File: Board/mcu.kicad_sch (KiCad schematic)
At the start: 20 parts, among them J2 Conn_01x03_Pin, Q1 BSS138, U2 RP2040

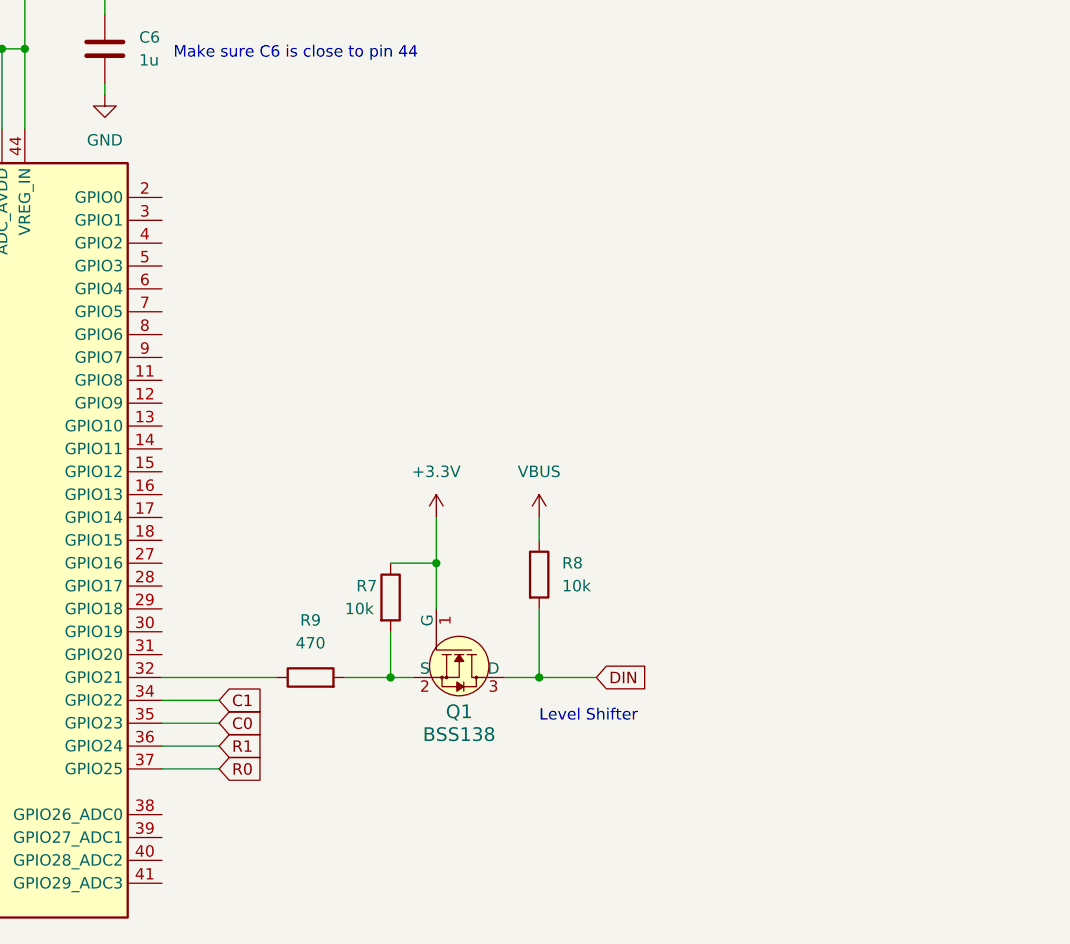
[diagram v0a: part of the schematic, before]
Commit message: Change led decoupler type
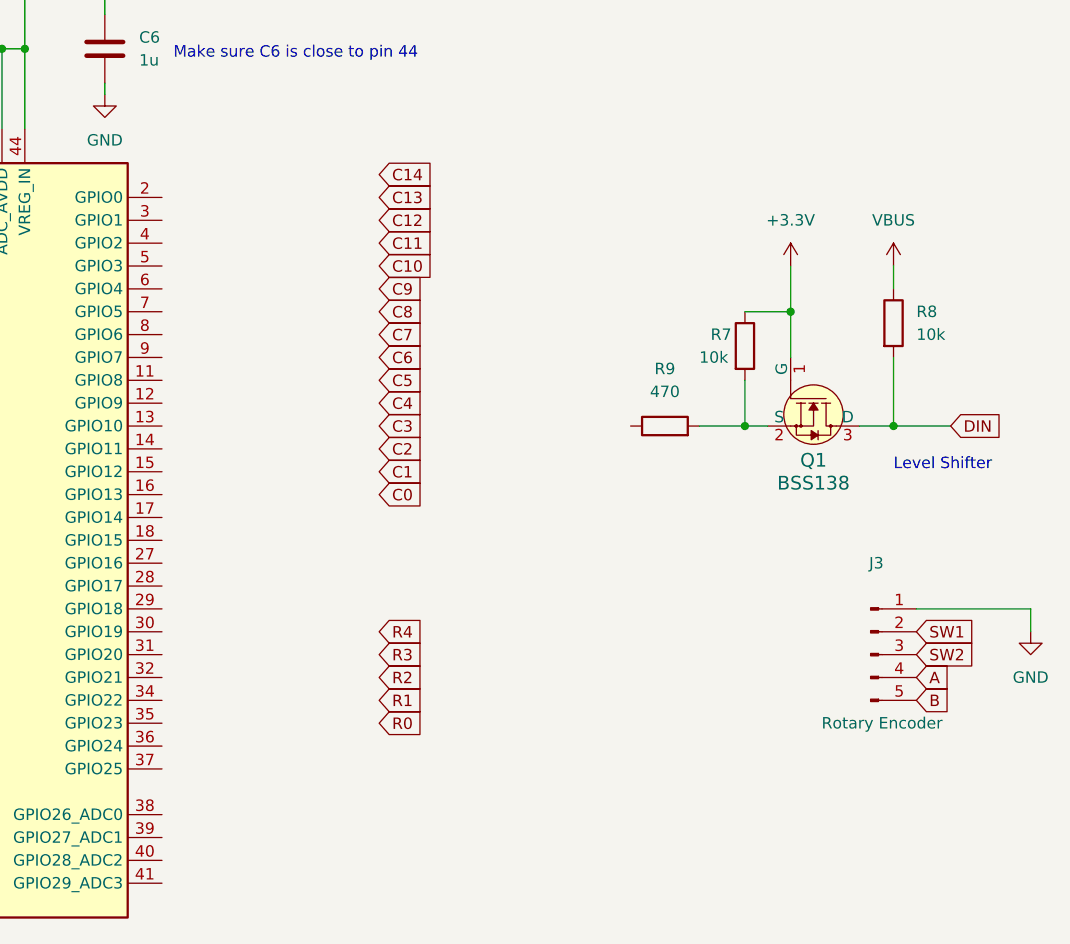
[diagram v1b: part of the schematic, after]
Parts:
- added J3: Conn_01x05_Pin, Connector_PinHeader_2.54mm:PinHeader_1x05_P2.54mm_Vertical, symbol Connector:Conn_01x05_Pin
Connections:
- net C0: no longer U2.35 (GPIO23)
- net C1: no longer U2.34 (GPIO22)
- net GND: now also J3.1 (Pin_1)
- net R0: no longer U2.37 (GPIO25)
- net R1: no longer U2.36 (GPIO24)
- net at R9.1: no longer U2.32 (GPIO21)
- new net A: J3.4 (Pin_4)
- new net B: J3.5 (Pin_5)
- new net SW1: J3.2 (Pin_2)
- new net SW2: J3.3 (Pin_3)
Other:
- moved on the sheet: Q1, R7, R8, R9

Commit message: Backing up"
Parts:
- Q1: footprint digikey-footprints:SOT-23-3 -> Package_TO_SOT_SMD:SOT-23-3
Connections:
- net A: now also U2.35 (GPIO23)
- net B: now also U2.34 (GPIO22)
- net SW1: now also U2.37 (GPIO25)
- net SW2: now also U2.36 (GPIO24)
- net LED: now reaches R9.1
- net LED: now also U2.32 (GPIO21)
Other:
- moved on the sheet: J3
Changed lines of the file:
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@@
     (stroke (width 0) (type default))
   )
-  (wire (pts (xy 232.41 125.73) (xy 232.41 128.27))
+  (wire (pts (xy 172.72 148.59) (xy 172.72 151.13))
     (stroke (width 0) (type default))
   )
@@
     (stroke (width 0) (type default))
   )
+  (wire (pts (xy 135.89 138.43) (xy 139.7 138.43))
+    (stroke (width 0) (type default))
+  )
   (wire (pts (xy 189.23 41.91) (xy 201.93 41.91))
     (stroke (width 0) (type default))
@@
     (stroke (width 0) (type default))
   )
+  (wire (pts (xy 135.89 140.97) (xy 139.7 140.97))
+    (stroke (width 0) (type default))
+  )
   (wire (pts (xy 118.11 63.5) (xy 118.11 72.39))
     (stroke (width 0) (type default))
@@
     (stroke (width 0) (type default))
   )
+  (wire (pts (xy 135.89 133.35) (xy 139.7 133.35))
+    (stroke (width 0) (type default))
+  )
   (wire (pts (xy 200.66 100.33) (xy 200.66 105.41))
     (stroke (width 0) (type default))
@@
     (stroke (width 0) (type default))
   )
+  (wire (pts (xy 135.89 143.51) (xy 139.7 143.51))
+    (stroke (width 0) (type default))
+  )
   (wire (pts (xy 38.1 152.4) (xy 38.1 149.86))
     (stroke (width 0) (type default))
@@
     (stroke (width 0) (type default))
   )
+  (wire (pts (xy 185.42 105.41) (xy 187.96 105.41))
+    (stroke (width 0) (type default))
+  )
   (wire (pts (xy 200.66 105.41) (xy 203.2 105.41))
     (stroke (width 0) (type default))
@@
     (stroke (width 0) (type default))
   )
+  (wire (pts (xy 135.89 135.89) (xy 139.7 135.89))
+    (stroke (width 0) (type default))
+  )
   (wire (pts (xy 115.57 63.5) (xy 113.03 63.5))
     (stroke (width 0) (type default))
@@
     (stroke (width 0) (type default))
   )
-  (wire (pts (xy 219.71 125.73) (xy 232.41 125.73))
+  (wire (pts (xy 160.02 148.59) (xy 172.72 148.59))
     (stroke (width 0) (type default))
   )
@@
     )
   )
-  (global_label "SW2" (shape input) (at 219.71 130.81 0) (fields_autoplaced)
-    (effects (font (size 1.27 1.27)) (justify left))
-    (property "Intersheetrefs" "${INTERSHEET_REFS}" (at 226.5656 130.81 0)
+  (global_label "SW2" (shape input) (at 160.02 153.67 0) (fields_autoplaced)
+    (effects (font (size 1.27 1.27)) (justify left))
+    (property "Intersheetrefs" "${INTERSHEET_REFS}" (at 166.8756 153.67 0)
       (effects (font (size 1.27 1.27)) (justify left) hide)
     )
@@
     )
   )
+  (global_label "LED" (shape input) (at 185.42 105.41 180) (fields_autoplaced)
+    (effects (font (size 1.27 1.27)) (justify right))
+    (property "Intersheetrefs" "${INTERSHEET_REFS}" (at 178.9877 105.41 0)
+      (effects (font (size 1.27 1.27)) (justify right) hide)
+    )
+  )
   (global_label "XOUT" (shape input) (at 82.55 135.89 180) (fields_autoplaced)
     (effects (font (size 1.27 1.27)) (justify right))
@@
     )
   )
+  (global_label "A" (shape input) (at 139.7 138.43 0) (fields_autoplaced)
+    (effects (font (size 1.27 1.27)) (justify left))
+    (property "Intersheetrefs" "${INTERSHEET_REFS}" (at 143.7738 138.43 0)
+      (effects (font (size 1.27 1.27)) (justify left) hide)
+    )
+  )
   (global_label "C0" (shape input) (at 160.02 113.03 0) (fields_autoplaced)
     (effects (font (size 1.27 1.27)) (justify left))
@@
     )
   )
-  (global_label "A" (shape input) (at 219.71 133.35 0) (fields_autoplaced)
-    (effects (font (size 1.27 1.27)) (justify left))
-    (property "Intersheetrefs" "${INTERSHEET_REFS}" (at 223.7838 133.35 0)
+  (global_label "A" (shape input) (at 160.02 156.21 0) (fields_autoplaced)
+    (effects (font (size 1.27 1.27)) (justify left))
+    (property "Intersheetrefs" "${INTERSHEET_REFS}" (at 164.0938 156.21 0)
+      (effects (font (size 1.27 1.27)) (justify left) hide)
+    )
+  )
+  (global_label "LED" (shape input) (at 139.7 133.35 0) (fields_autoplaced)
+    (effects (font (size 1.27 1.27)) (justify left))
+    (property "Intersheetrefs" "${INTERSHEET_REFS}" (at 146.1323 133.35 0)
       (effects (font (size 1.27 1.27)) (justify left) hide)
     )
@@
     )
   )
+  (global_label "B" (shape input) (at 139.7 135.89 0) (fields_autoplaced)
+    (effects (font (size 1.27 1.27)) (justify left))
+    (property "Intersheetrefs" "${INTERSHEET_REFS}" (at 143.9552 135.89 0)
+      (effects (font (size 1.27 1.27)) (justify left) hide)
+    )
+  )
   (global_label "QSPI_SD0" (shape input) (at 64.77 102.87 180) (fields_autoplaced)
     (effects (font (size 1.27 1.27)) (justify right))
@@
     )
   )
+  (global_label "SW2" (shape input) (at 139.7 140.97 0) (fields_autoplaced)
+    (effects (font (size 1.27 1.27)) (justify left))
+    (property "Intersheetrefs" "${INTERSHEET_REFS}" (at 146.5556 140.97 0)
+      (effects (font (size 1.27 1.27)) (justify left) hide)
+    )
+  )
+  (global_label "SW1" (shape input) (at 139.7 143.51 0) (fields_autoplaced)
+    (effects (font (size 1.27 1.27)) (justify left))
+    (property "Intersheetrefs" "${INTERSHEET_REFS}" (at 146.5556 143.51 0)
+      (effects (font (size 1.27 1.27)) (justify left) hide)
+    )
+  )
   (global_label "C6" (shape input) (at 160.02 97.79 0) (fields_autoplaced)
     (effects (font (size 1.27 1.27)) (justify left))
@@
     )
   )
-  (global_label "SW1" (shape input) (at 219.71 128.27 0) (fields_autoplaced)
-    (effects (font (size 1.27 1.27)) (justify left))
-    (property "Intersheetrefs" "${INTERSHEET_REFS}" (at 226.5656 128.27 0)
+  (global_label "SW1" (shape input) (at 160.02 151.13 0) (fields_autoplaced)
+    (effects (font (size 1.27 1.27)) (justify left))
+    (property "Intersheetrefs" "${INTERSHEET_REFS}" (at 166.8756 151.13 0)
       (effects (font (size 1.27 1.27)) (justify left) hide)
     )
@@
     )
   )
-  (global_label "B" (shape input) (at 219.71 135.89 0) (fields_autoplaced)
-    (effects (font (size 1.27 1.27)) (justify left))
-    (property "Intersheetrefs" "${INTERSHEET_REFS}" (at 223.9652 135.89 0)
+  (global_label "B" (shape input) (at 160.02 158.75 0) (fields_autoplaced)
+    (effects (font (size 1.27 1.27)) (justify left))
+    (property "Intersheetrefs" "${INTERSHEET_REFS}" (at 164.2752 158.75 0)
       (effects (font (size 1.27 1.27)) (justify left) hide)
     )
@@
     )
   )
-  (symbol (lib_id "Connector:Conn_01x05_Pin") (at 214.63 130.81 0) (unit 1)
+  (symbol (lib_id "Connector:Conn_01x05_Pin") (at 154.94 153.67 0) (unit 1)
     (in_bom yes) (on_board yes) (dnp no)
-    (property "Reference" "J3" (at 215.265 120.65 0)
-      (effects (font (size 1.27 1.27)))
-    )
-    (property "Value" "Conn_01x05_Pin" (at 215.265 123.19 0)
-      (effects (font (size 1.27 1.27)) hide)
-    )
-    (property "Footprint" "Connector_PinHeader_2.54mm:PinHeader_1x05_P2.54mm_Vertical" (at 214.63 130.81 0)
-      (effects (font (size 1.27 1.27)) hide)
-    )
-    (property "Datasheet" "~" (at 214.63 130.81 0)
-      (effects (font (size 1.27 1.27)) hide)
-    )
-    (property "Name" "Rotary Encoder" (at 215.9 138.43 0)
+    (property "Reference" "J3" (at 155.575 143.51 0)
+      (effects (font (size 1.27 1.27)))
+    )
+    (property "Value" "Conn_01x05_Pin" (at 155.575 146.05 0)
+      (effects (font (size 1.27 1.27)) hide)
+    )
+    (property "Footprint" "Connector_PinHeader_2.54mm:PinHeader_1x05_P2.54mm_Vertical" (at 154.94 153.67 0)
+      (effects (font (size 1.27 1.27)) hide)
+    )
+    (property "Datasheet" "~" (at 154.94 153.67 0)
+      (effects (font (size 1.27 1.27)) hide)
+    )
+    (property "Name" "Rotary Encoder" (at 156.21 161.29 0)
       (effects (font (size 1.27 1.27)))
     )
@@
     )
   )
-  (symbol (lib_id "power:GND") (at 232.41 128.27 0) (unit 1)
-    (in_bom yes) (on_board yes) (dnp no) (fields_autoplaced)
-    (property "Reference" "#PWR0170" (at 232.41 134.62 0)
-      (effects (font (size 1.27 1.27)) hide)
-    )
-    (property "Value" "GND" (at 232.41 133.35 0)
-      (effects (font (size 1.27 1.27)))
-    )
-    (property "Footprint" "" (at 232.41 128.27 0)
-      (effects (font (size 1.27 1.27)) hide)
-    )
-    (property "Datasheet" "" (at 232.41 128.27 0)
+  (symbol (lib_id "power:GND") (at 172.72 151.13 0) (unit 1)
+    (in_bom yes) (on_board yes) (dnp no) (fields_autoplaced)
+    (property "Reference" "#PWR0170" (at 172.72 157.48 0)
+      (effects (font (size 1.27 1.27)) hide)
+    )
+    (property "Value" "GND" (at 172.72 156.21 0)
+      (effects (font (size 1.27 1.27)))
+    )
+    (property "Footprint" "" (at 172.72 151.13 0)
+      (effects (font (size 1.27 1.27)) hide)
+    )
+    (property "Datasheet" "" (at 172.72 151.13 0)
       (effects (font (size 1.27 1.27)) hide)
     )
@@
       (effects (font (size 1.524 1.524)))
     )
-    (property "Footprint" "digikey-footprints:SOT-23-3" (at 213.36 110.49 0)
+    (property "Footprint" "Package_TO_SOT_SMD:SOT-23-3" (at 213.36 110.49 0)
       (effects (font (size 1.524 1.524)) (justify left) hide)
     )
@@
   )
   (symbol (lib_id "MCU_RaspberryPi:RP2040") (at 110.49 118.11 0) (unit 1)
-    (in_bom yes) (on_board yes) (dnp no) (fields_autoplaced)
+    (in_bom yes) (on_board yes) (dnp no)
     (property "Reference" "U2" (at 112.6841 162.56 0)
       (effects (font (size 1.27 1.27)) (justify left))

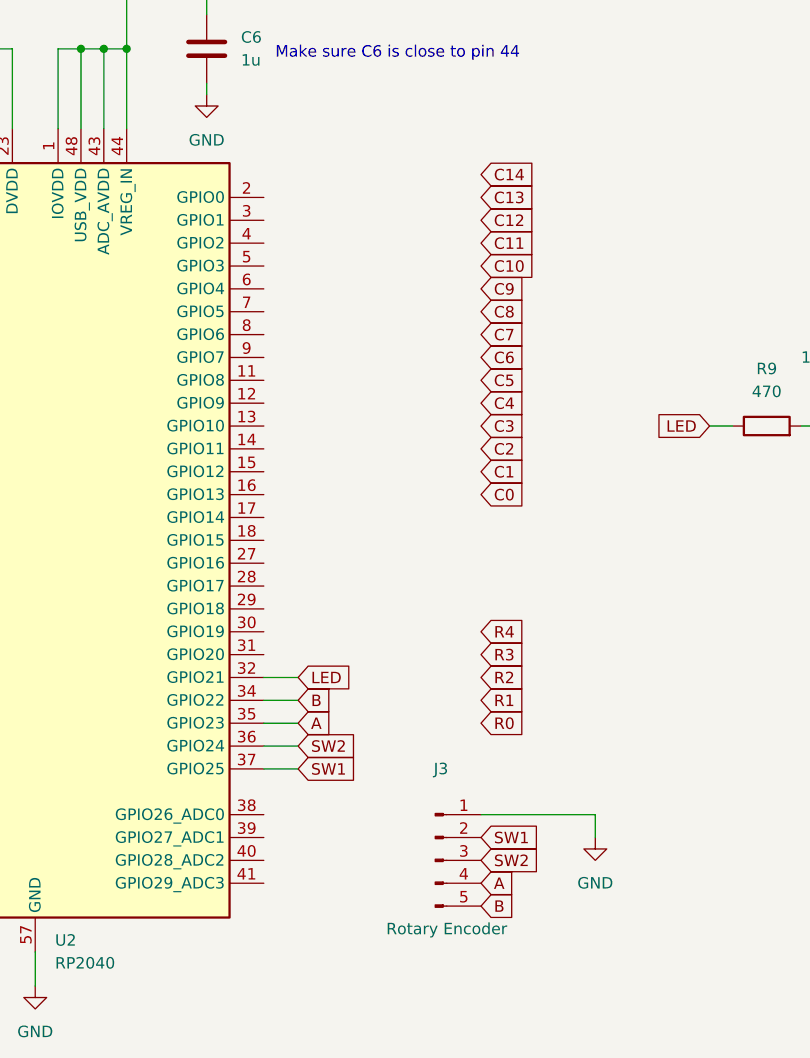
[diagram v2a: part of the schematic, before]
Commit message: Finish routing key matrix
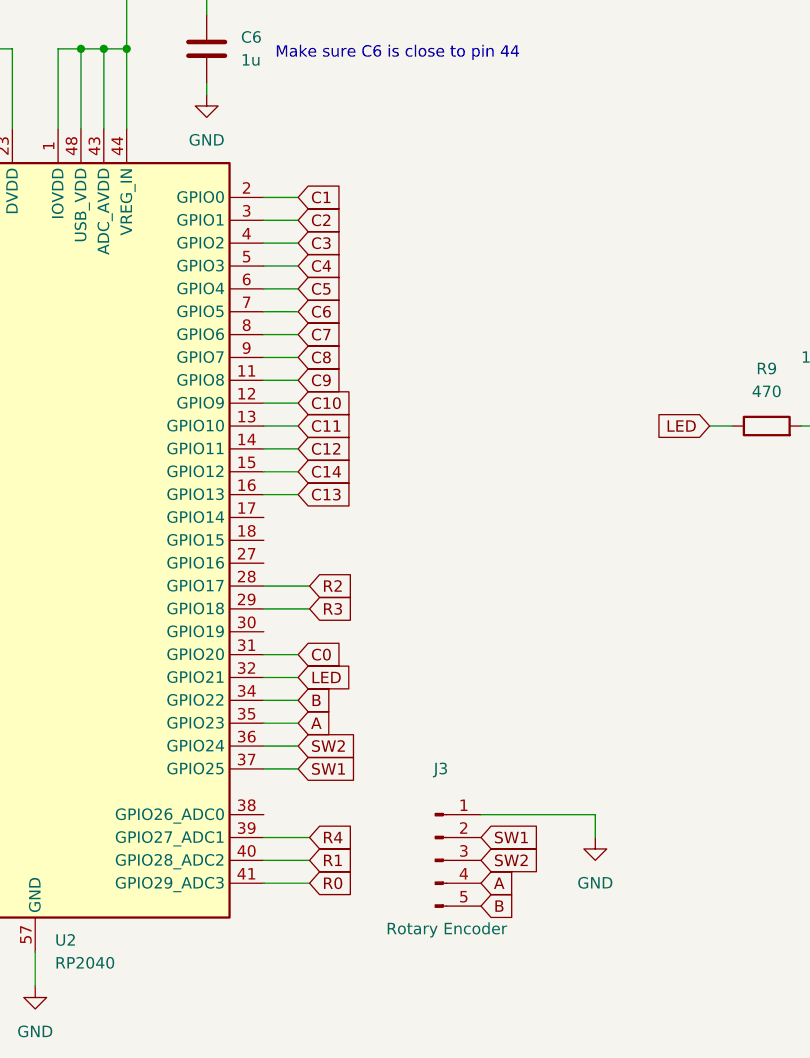
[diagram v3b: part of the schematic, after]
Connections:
- net C0: now also U2.31 (GPIO20)
- net C1: now also U2.2 (GPIO0)
- net C10: now also U2.12 (GPIO9)
- net C11: now also U2.13 (GPIO10)
- net C12: now also U2.14 (GPIO11)
- net C13: now also U2.16 (GPIO13)
- net C14: now also U2.15 (GPIO12)
- net C2: now also U2.3 (GPIO1)
- net C3: now also U2.4 (GPIO2)
- net C4: now also U2.5 (GPIO3)
- net C5: now also U2.6 (GPIO4)
- net C6: now also U2.7 (GPIO5)
- net C7: now also U2.8 (GPIO6)
- net C8: now also U2.9 (GPIO7)
- net C9: now also U2.11 (GPIO8)
- net R0: now also U2.41 (GPIO29_ADC3)
- net R1: now also U2.40 (GPIO28_ADC2)
- net R2: now also U2.28 (GPIO17)
- net R3: now also U2.29 (GPIO18)
- net R4: now also U2.39 (GPIO27_ADC1)

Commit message: Finish rev1
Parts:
- added D69: SJD12A06L01, Diode_SMD:D_SOD-123, symbol Diode:SMF54A
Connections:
- net GND: now also D69.2 (A2)
- net VBUS: now also D69.1 (A1)
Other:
- note added: "ESD Protection"
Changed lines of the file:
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@@
+    (stroke (width 0) (type default))
+  )
+  (wire (pts (xy 199.39 127) (xy 199.39 128.27))
     (stroke (width 0) (type default))
   )
@@
   )
   (wire (pts (xy 163.83 49.53) (xy 176.53 49.53))
+    (stroke (width 0) (type default))
+  )
+  (wire (pts (xy 199.39 137.16) (xy 199.39 135.89))
     (stroke (width 0) (type default))
   )
@@
   )
   (text "Make sure C6 is close to pin 44\n" (at 137.16 64.77 0)
+    (effects (font (size 1.27 1.27)) (justify left bottom))
+  )
+  (text "ESD Protection" (at 201.93 138.43 0)
     (effects (font (size 1.27 1.27)) (justify left bottom))
   )
@@
     )
   )
+  (symbol (lib_id "power:GND") (at 199.39 137.16 0) (unit 1)
+    (in_bom yes) (on_board yes) (dnp no) (fields_autoplaced)
+    (property "Reference" "#PWR0172" (at 199.39 143.51 0)
+      (effects (font (size 1.27 1.27)) hide)
+    )
+    (property "Value" "GND" (at 199.39 142.24 0)
+      (effects (font (size 1.27 1.27)))
+    )
+    (property "Footprint" "" (at 199.39 137.16 0)
+      (effects (font (size 1.27 1.27)) hide)
+    )
+    (property "Datasheet" "" (at 199.39 137.16 0)
+      (effects (font (size 1.27 1.27)) hide)
+    )
+    (pin "1")
+    (instances
+      (project "ND68"
+        (path "/f6515d16-f8c0-46c5-adb6-b60d73ae282b/d4ffdf96-4dca-426a-a450-916a785fbc50"
+          (reference "#PWR0172") (unit 1)
+        )
+      )
+    )
+  )
   (symbol (lib_id "Device:C") (at 38.1 146.05 0) (unit 1)
     (in_bom yes) (on_board yes) (dnp no) (fields_autoplaced)
@@
         (path "/f6515d16-f8c0-46c5-adb6-b60d73ae282b/d4ffdf96-4dca-426a-a450-916a785fbc50"
           (reference "C12") (unit 1)
+        )
+      )
+    )
+  )
+  (symbol (lib_id "Diode:SMF54A") (at 199.39 132.08 270) (unit 1)
+    (in_bom yes) (on_board yes) (dnp no) (fields_autoplaced)
+    (property "Reference" "D69" (at 201.93 130.81 90)
+      (effects (font (size 1.27 1.27)) (justify left))
+    )
+    (property "Value" "SJD12A06L01" (at 201.93 133.35 90)
+      (effects (font (size 1.27 1.27)) (justify left))
+    )
+    (property "Footprint" "Diode_SMD:D_SOD-123" (at 194.31 132.08 0)
+      (effects (font (size 1.27 1.27)) hide)
+    )
+    (property "Datasheet" "https://www.vishay.com/doc?85881" (at 199.39 130.81 0)
+      (effects (font (size 1.27 1.27)) hide)
+    )
+    (property "DigiKey" "YAG6686CT-ND" (at 199.39 132.08 0)
+      (effects (font (size 1.27 1.27)) hide)
+    )
+    (pin "1")
+    (pin "2")
+    (instances
+      (project "ND68"
+        (path "/f6515d16-f8c0-46c5-adb6-b60d73ae282b/d4ffdf96-4dca-426a-a450-916a785fbc50"
+          (reference "D69") (unit 1)
         )
       )
@@
         )
       )
+    )
+  )
+  (symbol (lib_id "power:VBUS") (at 199.39 127 0) (unit 1)
+    (in_bom yes) (on_board yes) (dnp no) (fields_autoplaced)
+    (property "Reference" "#PWR0171" (at 199.39 130.81 0)
+      (effects (font (size 1.27 1.27)) hide)
+    )
+    (property "Value" "VBUS" (at 199.39 121.92 0)
+      (effects (font (size 1.27 1.27)))
+    )
+    (property "Footprint" "" (at 199.39 127 0)
+      (effects (font (size 1.27 1.27)) hide)
+    )
+    (property "Datasheet" "" (at 199.39 127 0)
+      (effects (font (size 1.27 1.27)) hide)
+    )
+    (pin "1")
+    (instances
+      (project "ND68"
+        (path "/f6515d16-f8c0-46c5-adb6-b60d73ae282b/d4ffdf96-4dca-426a-a450-916a785fbc50"
+          (reference "#PWR0171") (unit 1)
+        )
+      )
